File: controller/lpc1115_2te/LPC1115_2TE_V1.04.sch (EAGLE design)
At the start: 59 parts, among them IC1 LPC1115, IC2 BD9G101, Q1 BC856, Q2 BC847C, Q3 BCP52, Q4 ASFL

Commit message: Id-resistor package changed to 1206 and replace.
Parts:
- R19, R20: device rcl:R-EU_R0603 -> rcl:R-EU_R1206
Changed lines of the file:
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@@
 <part name="P+12" library="supply1" deviceset="+3V3" device=""/>
 <part name="GND12" library="supply1" deviceset="GND" device=""/>
-<part name="R19" library="rcl" deviceset="R-EU_" device="R0603" value="47k"/>
-<part name="R20" library="rcl" deviceset="R-EU_" device="R0603" value="47k"/>
+<part name="R19" library="rcl" deviceset="R-EU_" device="R1206" value="47k"/>
+<part name="R20" library="rcl" deviceset="R-EU_" device="R1206" value="47k"/>
 </parts>
 <sheets>

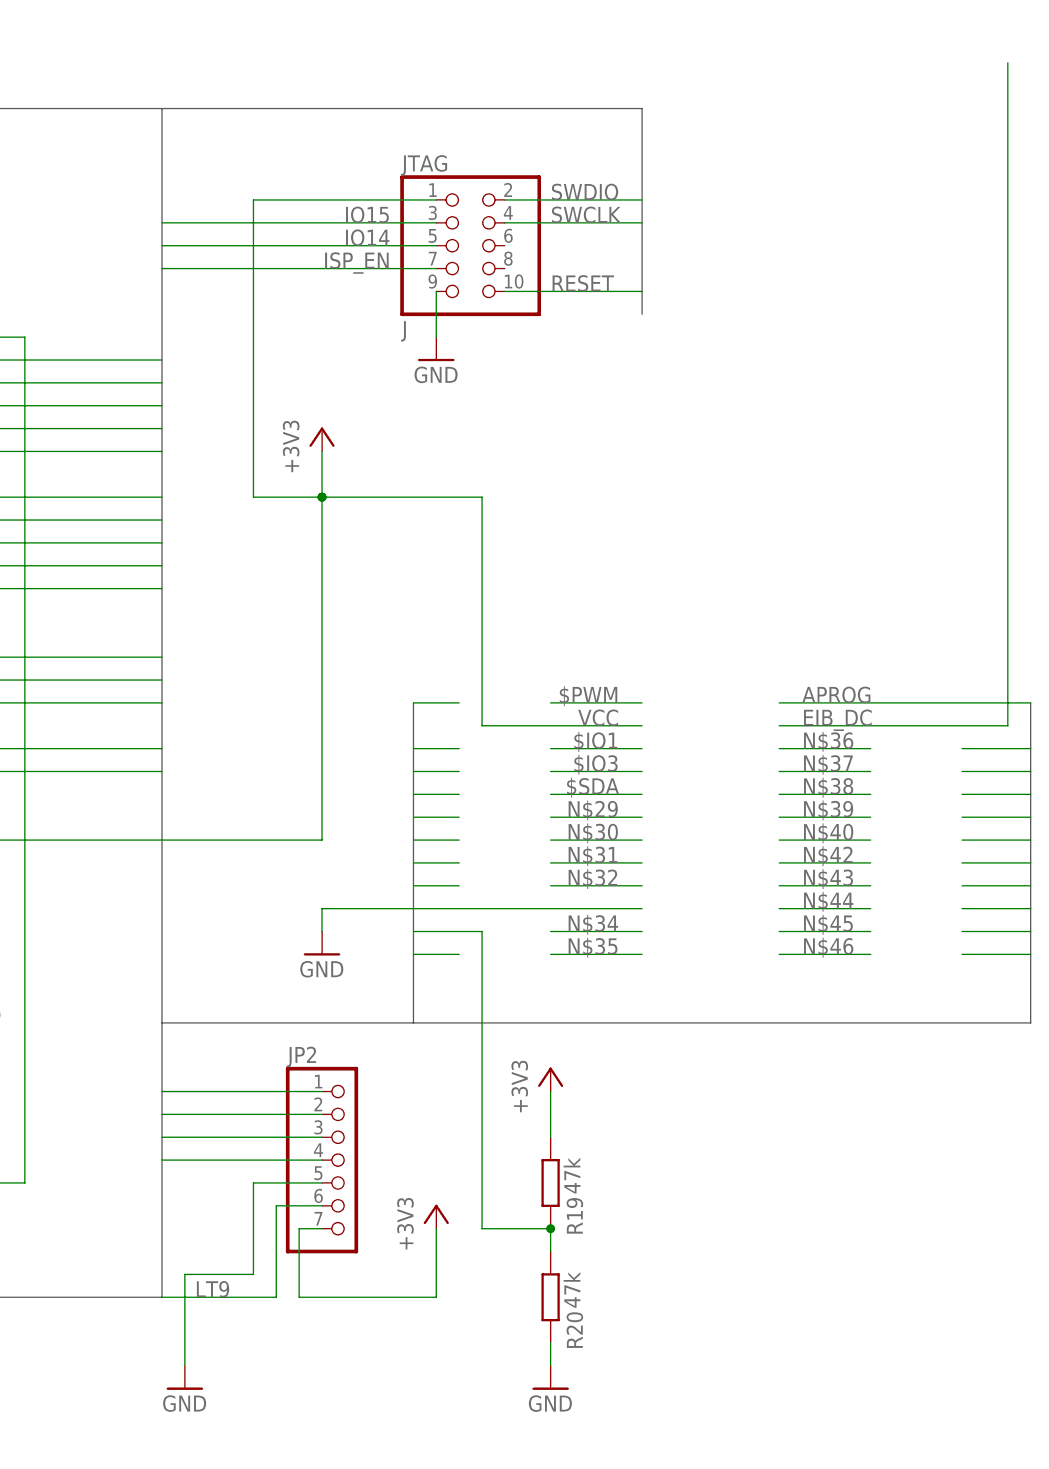
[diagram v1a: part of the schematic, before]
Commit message: IO / spi modify
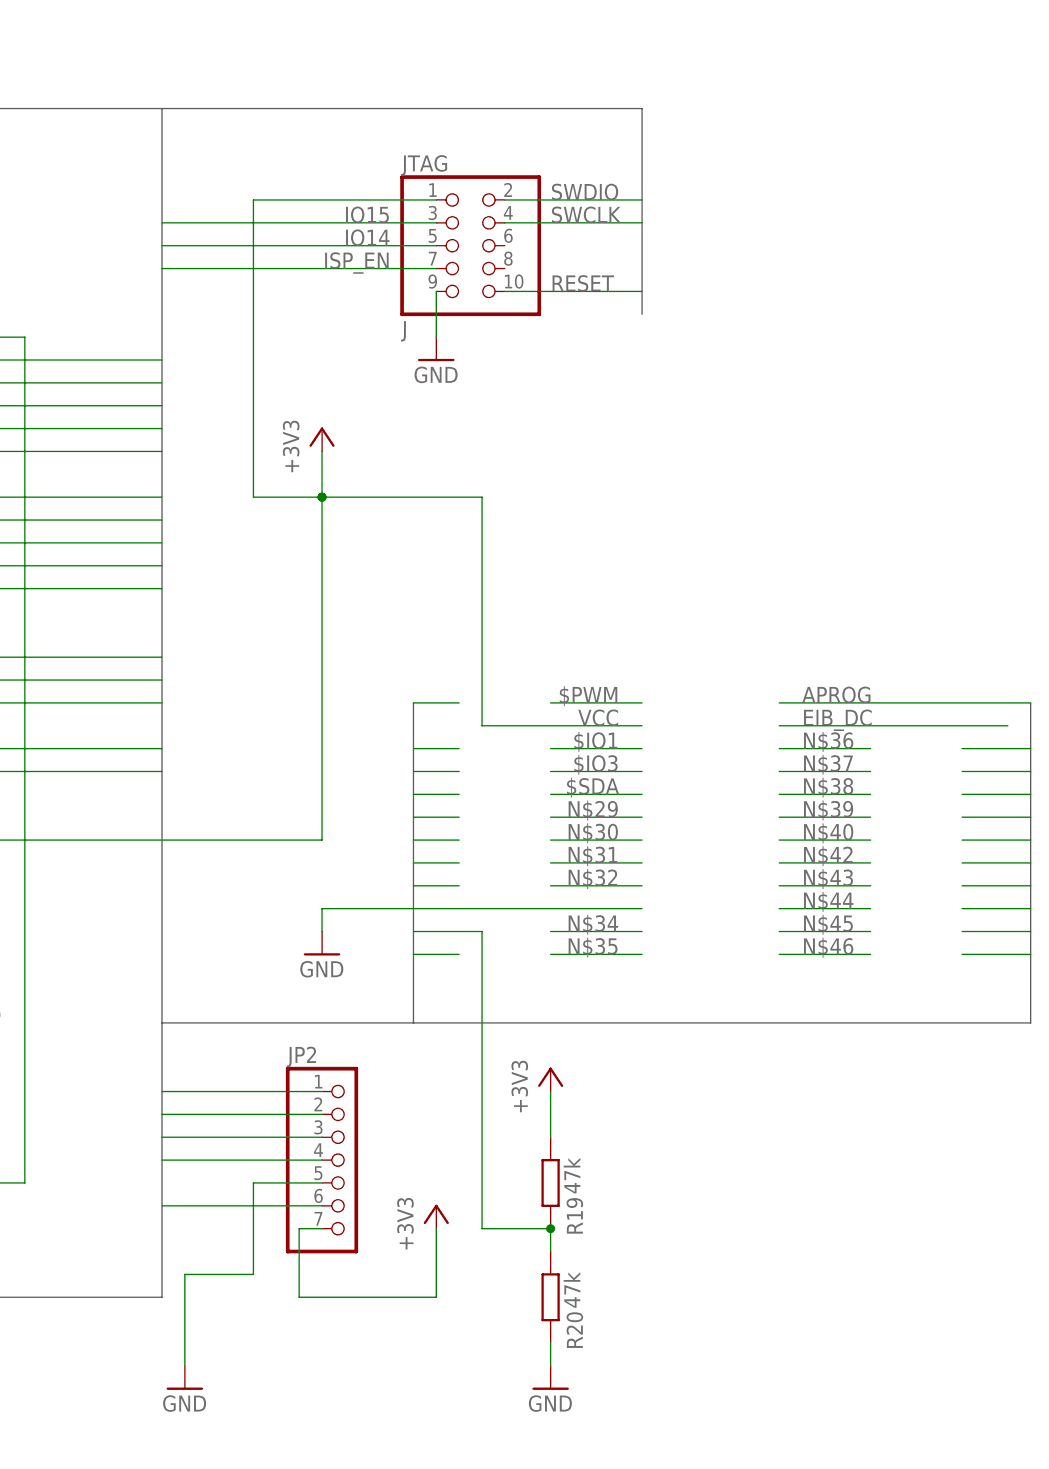
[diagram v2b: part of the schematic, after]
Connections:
- net IO4: no longer JP1.5
- net IO5: now also JP1.6
- net IO6: now also JP1.7
- net IO7: now also JP1.5; no longer JP1.7
- net IO8: no longer JP1.6
- net LT1: now also JP2.1
- net LT3: now also JP2.6
- net LT5: no longer JP2.1
- net LT8: no longer JP2.4
- net LT9: now also JP2.4; no longer JP2.6
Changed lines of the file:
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@@
 <grid distance="0.1" unitdist="inch" unit="inch" style="lines" multiple="1" display="no" altdistance="0.01" altunitdist="inch" altunit="inch"/>
 <layers>
-<layer number="1" name="Top" color="4" fill="1" visible="yes" active="no"/>
-<layer number="2" name="Route2" color="1" fill="3" visible="yes" active="no"/>
-<layer number="15" name="Route15" color="4" fill="6" visible="yes" active="no"/>
-<layer number="16" name="Bottom" color="1" fill="1" visible="yes" active="no"/>
-<layer number="17" name="Pads" color="2" fill="1" visible="yes" active="no"/>
-<layer number="18" name="Vias" color="2" fill="1" visible="yes" active="no"/>
-<layer number="19" name="Unrouted" color="6" fill="1" visible="yes" active="no"/>
-<layer number="20" name="Dimension" color="15" fill="1" visible="yes" active="no"/>
-<layer number="21" name="tPlace" color="7" fill="1" visible="yes" active="no"/>
-<layer number="22" name="bPlace" color="7" fill="1" visible="yes" active="no"/>
-<layer number="23" name="tOrigins" color="15" fill="1" visible="yes" active="no"/>
-<layer number="24" name="bOrigins" color="15" fill="1" visible="yes" active="no"/>
-<layer number="25" name="tNames" color="7" fill="1" visible="yes" active="no"/>
-<layer number="26" name="bNames" color="7" fill="1" visible="yes" active="no"/>
-<layer number="27" name="tValues" color="7" fill="1" visible="yes" active="no"/>
-<layer number="28" name="bValues" color="7" fill="1" visible="yes" active="no"/>
+<layer number="1" name="Top" color="4" fill="1" visible="no" active="no"/>
+<layer number="2" name="Route2" color="1" fill="3" visible="no" active="no"/>
+<layer number="15" name="Route15" color="4" fill="6" visible="no" active="no"/>
+<layer number="16" name="Bottom" color="1" fill="1" visible="no" active="no"/>
+<layer number="17" name="Pads" color="2" fill="1" visible="no" active="no"/>
+<layer number="18" name="Vias" color="2" fill="1" visible="no" active="no"/>
+<layer number="19" name="Unrouted" color="6" fill="1" visible="no" active="no"/>
+<layer number="20" name="Dimension" color="15" fill="1" visible="no" active="no"/>
+<layer number="21" name="tPlace" color="7" fill="1" visible="no" active="no"/>
+<layer number="22" name="bPlace" color="7" fill="1" visible="no" active="no"/>
+<layer number="23" name="tOrigins" color="15" fill="1" visible="no" active="no"/>
+<layer number="24" name="bOrigins" color="15" fill="1" visible="no" active="no"/>
+<layer number="25" name="tNames" color="7" fill="1" visible="no" active="no"/>
+<layer number="26" name="bNames" color="7" fill="1" visible="no" active="no"/>
+<layer number="27" name="tValues" color="7" fill="1" visible="no" active="no"/>
+<layer number="28" name="bValues" color="7" fill="1" visible="no" active="no"/>
 <layer number="29" name="tStop" color="7" fill="3" visible="no" active="no"/>
 <layer number="30" name="bStop" color="7" fill="6" visible="no" active="no"/>
@@
 <layer number="35" name="tGlue" color="7" fill="4" visible="no" active="no"/>
 <layer number="36" name="bGlue" color="7" fill="5" visible="no" active="no"/>
-<layer number="37" name="tTest" color="7" fill="1" visible="yes" active="no"/>
-<layer number="38" name="bTest" color="7" fill="1" visible="yes" active="no"/>
+<layer number="37" name="tTest" color="7" fill="1" visible="no" active="no"/>
+<layer number="38" name="bTest" color="7" fill="1" visible="no" active="no"/>
 <layer number="39" name="tKeepout" color="4" fill="11" visible="no" active="no"/>
 <layer number="40" name="bKeepout" color="1" fill="11" visible="no" active="no"/>
@@
 <layer number="44" name="Drills" color="7" fill="1" visible="no" active="no"/>
 <layer number="45" name="Holes" color="7" fill="1" visible="no" active="no"/>
-<layer number="46" name="Milling" color="3" fill="1" visible="yes" active="no"/>
-<layer number="47" name="Measures" color="7" fill="1" visible="yes" active="no"/>
-<layer number="48" name="Document" color="7" fill="1" visible="yes" active="no"/>
-<layer number="49" name="Reference" color="7" fill="1" visible="yes" active="no"/>
-<layer number="50" name="dxf" color="7" fill="1" visible="yes" active="no"/>
-<layer number="51" name="tDocu" color="7" fill="1" visible="yes" active="no"/>
-<layer number="52" name="bDocu" color="7" fill="1" visible="yes" active="no"/>
-<layer number="53" name="tGND_GNDA" color="7" fill="9" visible="yes" active="no"/>
-<layer number="54" name="bGND_GNDA" color="1" fill="9" visible="yes" active="no"/>
-<layer number="56" name="wert" color="7" fill="1" visible="yes" active="no"/>
+<layer number="46" name="Milling" color="3" fill="1" visible="no" active="no"/>
+<layer number="47" name="Measures" color="7" fill="1" visible="no" active="no"/>
+<layer number="48" name="Document" color="7" fill="1" visible="no" active="no"/>
+<layer number="49" name="Reference" color="7" fill="1" visible="no" active="no"/>
+<layer number="50" name="dxf" color="7" fill="1" visible="no" active="no"/>
+<layer number="51" name="tDocu" color="7" fill="1" visible="no" active="no"/>
+<layer number="52" name="bDocu" color="7" fill="1" visible="no" active="no"/>
+<layer number="53" name="tGND_GNDA" color="7" fill="9" visible="no" active="no"/>
+<layer number="54" name="bGND_GNDA" color="1" fill="9" visible="no" active="no"/>
+<layer number="56" name="wert" color="7" fill="1" visible="no" active="no"/>
 <layer number="91" name="Nets" color="2" fill="1" visible="yes" active="yes"/>
 <layer number="92" name="Busses" color="1" fill="1" visible="yes" active="yes"/>
@@
 <segment>
 <wire x1="391.16" y1="139.7" x2="416.56" y2="139.7" width="0.1524" layer="91"/>
-<wire x1="416.56" y1="139.7" x2="416.56" y2="213.36" width="0.1524" layer="91"/>
 <label x="393.7" y="139.7" size="1.778" layer="95"/>
 </segment>
@@
 <label x="297.18" y="180.34" size="1.778" layer="95"/>
 </segment>
+<segment>
+<pinref part="JP2" gate="A" pin="1"/>
+<wire x1="322.58" y1="99.06" x2="340.36" y2="99.06" width="0.1524" layer="91"/>
+</segment>
 </net>
 <net name="LT2" class="0">
@@
 <label x="297.18" y="172.72" size="1.778" layer="95"/>
 </segment>
+<segment>
+<pinref part="JP2" gate="A" pin="6"/>
+<wire x1="322.58" y1="86.36" x2="340.36" y2="86.36" width="0.1524" layer="91"/>
+</segment>
 </net>
 <net name="LT5" class="0">
@@
 <label x="297.18" y="134.62" size="1.778" layer="95"/>
 </segment>
-<segment>
-<wire x1="322.58" y1="99.06" x2="340.36" y2="99.06" width="0.1524" layer="91"/>
-<pinref part="JP2" gate="A" pin="1"/>
-</segment>
 </net>
 <net name="IO8" class="0">
@@
 <wire x1="411.48" y1="127" x2="419.1" y2="127" width="0.1524" layer="91"/>
 </segment>
-<segment>
-<pinref part="JP1" gate="A" pin="6"/>
-<wire x1="33.02" y1="71.12" x2="25.4" y2="71.12" width="0.1524" layer="91"/>
-</segment>
 </net>
 <net name="IO1" class="0">
@@
 <label x="203.2" y="154.94" size="1.778" layer="95" rot="MR0"/>
 </segment>
-<segment>
-<wire x1="322.58" y1="91.44" x2="340.36" y2="91.44" width="0.1524" layer="91"/>
-<pinref part="JP2" gate="A" pin="4"/>
-</segment>
 </net>
 <net name="IO4" class="0">
@@
 <label x="297.18" y="160.02" size="1.778" layer="95"/>
 </segment>
-<segment>
-<pinref part="JP1" gate="A" pin="5"/>
-<wire x1="33.02" y1="73.66" x2="25.4" y2="73.66" width="0.1524" layer="91"/>
-</segment>
 </net>
 <net name="IO5" class="0">
@@
 <wire x1="355.6" y1="129.54" x2="350.52" y2="129.54" width="0.1524" layer="91"/>
 </segment>
+<segment>
+<pinref part="JP1" gate="A" pin="6"/>
+<wire x1="33.02" y1="71.12" x2="25.4" y2="71.12" width="0.1524" layer="91"/>
+</segment>
 </net>
 <net name="IO7" class="0">
@@
 </segment>
 <segment>
-<pinref part="JP1" gate="A" pin="7"/>
-<wire x1="33.02" y1="68.58" x2="25.4" y2="68.58" width="0.1524" layer="91"/>
+<pinref part="JP1" gate="A" pin="5"/>
+<wire x1="33.02" y1="73.66" x2="25.4" y2="73.66" width="0.1524" layer="91"/>
 </segment>
 </net>
@@
 </segment>
 <segment>
+<pinref part="JP2" gate="A" pin="2"/>
 <wire x1="322.58" y1="96.52" x2="340.36" y2="96.52" width="0.1524" layer="91"/>
-<pinref part="JP2" gate="A" pin="2"/>
 </segment>
 </net>
@@
 <net name="LT9" class="0">
 <segment>
-<label x="330.2" y="76.2" size="1.778" layer="95" rot="MR0"/>
-<wire x1="322.58" y1="76.2" x2="335.28" y2="76.2" width="0.1524" layer="91"/>
-<wire x1="335.28" y1="76.2" x2="335.28" y2="86.36" width="0.1524" layer="91"/>
-<wire x1="335.28" y1="86.36" x2="340.36" y2="86.36" width="0.1524" layer="91"/>
-<pinref part="JP2" gate="A" pin="6"/>
-</segment>
-<segment>
 <pinref part="IC1" gate="G$1" pin="PIO2_3/RI/MOSI1"/>
 <wire x1="322.58" y1="175.26" x2="294.64" y2="175.26" width="0.1524" layer="91"/>
 <label x="297.18" y="175.26" size="1.778" layer="95"/>
 </segment>
+<segment>
+<pinref part="JP2" gate="A" pin="4"/>
+<wire x1="322.58" y1="91.44" x2="340.36" y2="91.44" width="0.1524" layer="91"/>
+</segment>
 </net>
 <net name="SDA" class="0">
@@
 </segment>
 <segment>
+<pinref part="JP2" gate="A" pin="3"/>
 <wire x1="322.58" y1="93.98" x2="340.36" y2="93.98" width="0.1524" layer="91"/>
-<pinref part="JP2" gate="A" pin="3"/>
 </segment>
 </net>
@@
 <wire x1="411.48" y1="129.54" x2="419.1" y2="129.54" width="0.1524" layer="91"/>
 </segment>
-</net>
+<segment>
+<pinref part="JP1" gate="A" pin="7"/>
+<wire x1="33.02" y1="68.58" x2="25.4" y2="68.58" width="0.1524" layer="91"/>
+</segment>
+</net>
